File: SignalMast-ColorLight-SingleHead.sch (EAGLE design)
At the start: 4 parts

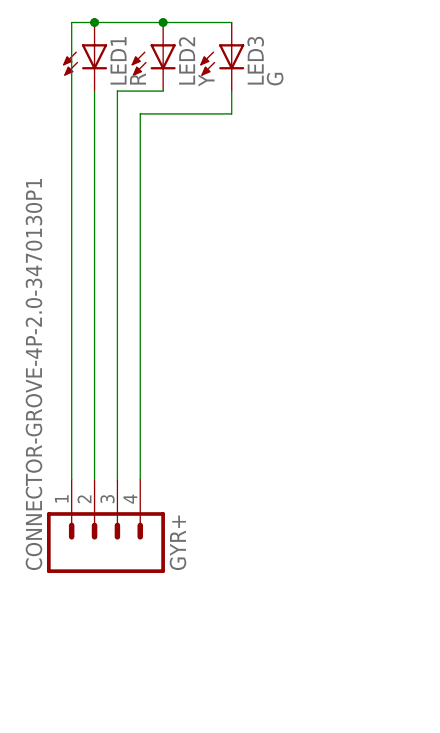
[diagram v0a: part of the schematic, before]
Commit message: normalized values
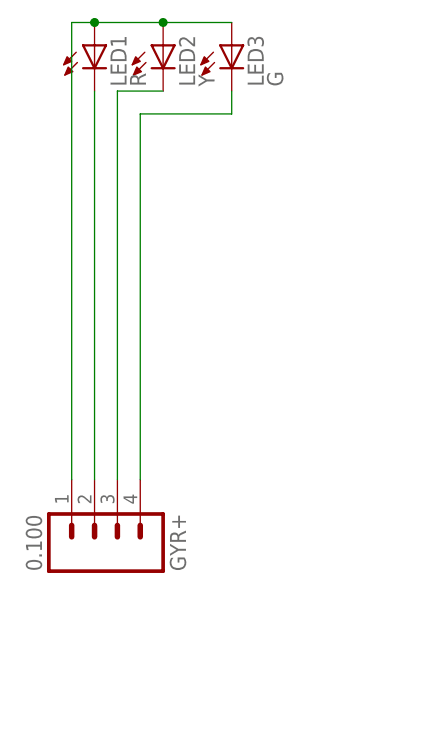
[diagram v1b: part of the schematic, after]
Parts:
- GYR+: value CONNECTOR-GROVE-4P-2.0-3470130P1 -> 0.100
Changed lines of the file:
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@@
 <parts>
 <part name="FRAME1" library="SPCoast" deviceset="DOC-FRAME-LETTER" device=""/>
-<part name="GYR+" library="SPCoast" deviceset="CONNECTOR-M04" device="LOCK" value="CONNECTOR-GROVE-4P-2.0-3470130P1"/>
+<part name="GYR+" library="SPCoast" deviceset="CONNECTOR-M04" device="LOCK" value="0.100"/>
 <part name="LED1" library="SPCoast" deviceset="LED*" device="0603-LED" value="R">
 <attribute name="OPL" value="19-217-R6C-AL1M2VY-3T"/>

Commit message: Version 1.3
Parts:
- renumbered GYR+ to J
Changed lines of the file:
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@@
 <layer number="255" name="routoute" color="7" fill="1" visible="yes" active="yes"/>
 </layers>
-<schematic xreflabel="%F%N/%S.%C%R" xrefpart="/%S.%C%R">
+<schematic xreflabel="%F%N/%S" xrefpart="/%S.%C%R">
 <attributes>
 </attributes>
@@
 <parts>
 <part name="FRAME1" library="SPCoast" deviceset="DOC-FRAME-LETTER" device=""/>
-<part name="GYR+" library="SPCoast" deviceset="CONNECTOR-M04" device="LOCK" value="0.100"/>
+<part name="J" library="SPCoast" deviceset="CONNECTOR-M04" device="LOCK" value="0.100"/>
 <part name="LED1" library="SPCoast" deviceset="LED*" device="0603-LED" value="R">
 <attribute name="OPL" value="19-217-R6C-AL1M2VY-3T"/>
@@
 <instance part="FRAME1" gate="FRAME" x="0" y="0"/>
 <instance part="FRAME1" gate="FRAME_CONTENT" x="147.32" y="0"/>
-<instance part="GYR+" gate="J" x="116.84" y="78.74" rot="MR90"/>
+<instance part="J" gate="J" x="116.84" y="78.74" rot="MR90"/>
 <instance part="LED1" gate="LED" x="116.84" y="129.54">
 <attribute name="OPL" x="116.84" y="129.54" size="1.778" layer="96" display="off"/>
@@
 <net name="BV+" class="0">
 <segment>
-<pinref part="GYR+" gate="J" pin="1"/>
+<pinref part="J" gate="J" pin="1"/>
 <wire x1="114.3" y1="83.82" x2="114.3" y2="134.62" width="0.1524" layer="91"/>
 <pinref part="LED1" gate="LED" pin="A"/>
@@
 <segment>
 <pinref part="LED1" gate="LED" pin="C"/>
-<pinref part="GYR+" gate="J" pin="2"/>
+<pinref part="J" gate="J" pin="2"/>
 <wire x1="116.84" y1="127" x2="116.84" y2="83.82" width="0.1524" layer="91"/>
 </segment>
@@
 <segment>
 <pinref part="LED2" gate="LED" pin="C"/>
-<pinref part="GYR+" gate="J" pin="3"/>
+<pinref part="J" gate="J" pin="3"/>
 <wire x1="124.46" y1="127" x2="119.38" y2="127" width="0.1524" layer="91"/>
 <wire x1="119.38" y1="127" x2="119.38" y2="83.82" width="0.1524" layer="91"/>
@@
 <pinref part="LED3" gate="LED" pin="C"/>
 <wire x1="132.08" y1="127" x2="132.08" y2="124.46" width="0.1524" layer="91"/>
-<pinref part="GYR+" gate="J" pin="4"/>
+<pinref part="J" gate="J" pin="4"/>
 <wire x1="132.08" y1="124.46" x2="121.92" y2="124.46" width="0.1524" layer="91"/>
 <wire x1="121.92" y1="124.46" x2="121.92" y2="83.82" width="0.1524" layer="91"/>
